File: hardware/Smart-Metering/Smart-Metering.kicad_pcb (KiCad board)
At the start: 4 copper layers, 130 x 130 mm, 230 parts, among them J101 AUX L N, J201 VA VB VC VN, J301 SENSOR_IA, J302 SENSOR_IB, J303 SENSOR_IC, J304 SENSOR_IN, J501 SWD, J701 HMI_LINK, J801 RS485, J802 USB-C, J901 BATTERY_1S, Q901 AO3401A, Q902 2N7002, SW901 POWER, U401 ADE9430ACPZ, U501 STM32F413RHT6, U502 24LC64, U601 ISO7762DW, U602 ISO7761DW, U604 MCP3204, U605 TPS7A2033PDBVR, U606 ADuM6000, U801 ADM2587E, U802 USBLC6-2SC6, U901 BQ25895RTW, U902 TPS63001, U903 TPS61022, Y401 24.576MHz, Y501 8MHz, Y502 32.768kHz

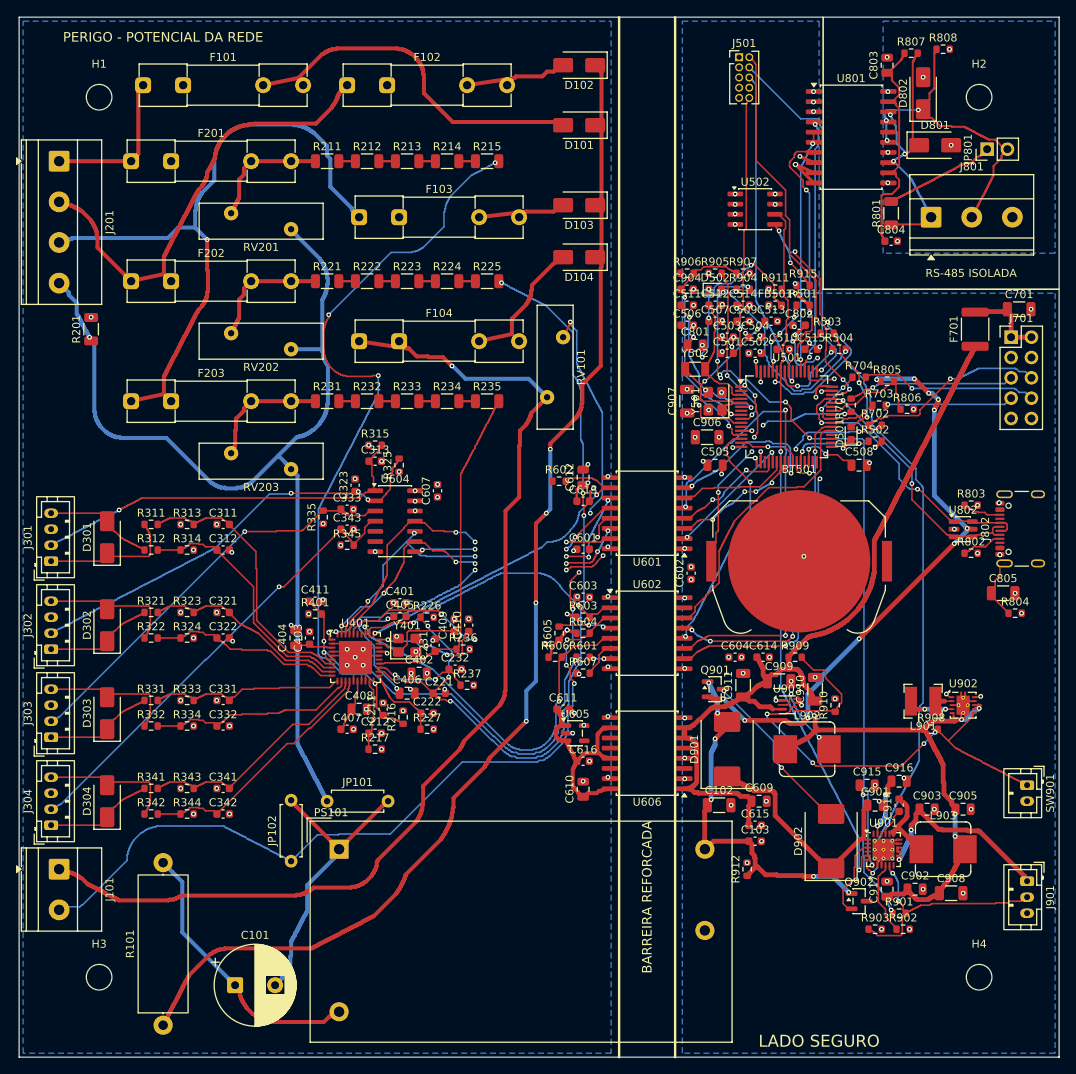
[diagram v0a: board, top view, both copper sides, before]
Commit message: Liga mais 8 pads pendentes da placa e atualiza a documentação
- reparo com vias menores (0,45/0,2 mm, 12 na placa), trechos de potência
  estreitados e reparo por grupo de pinos vizinhos; rodadas com ordens
  embaralhadas para o domínio quente;
- pendentes: 18 -> 10 (2 no domínio quente, 8 no lado seguro/RS-485),
  listados em docs/LAYOUT.md para ligar à mão;
- verificação geométrica da placa inteira: 0 violações; menor distância
  quente-seguro através da barreira: 8,02 mm;
- docs/LAYOUT.md: imagens da rev. 0.4 e seção de modelos 3D.

Co-Authored-By: Claude Opus 5.5 <noreply@anthropic.com>
Claude-Session: https://claude.ai/code/session_012B8cVkhtjf3eg98UdpNCpf
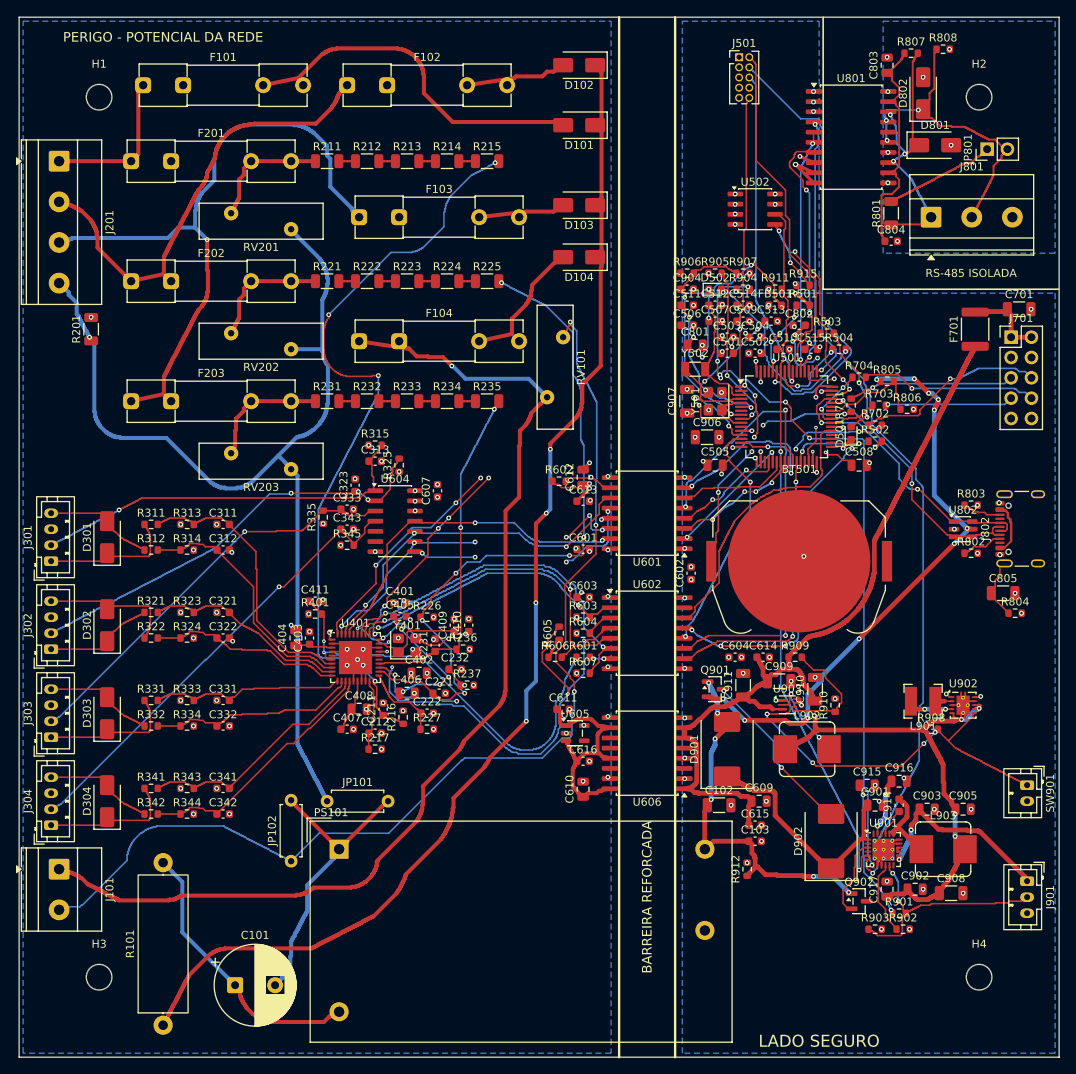
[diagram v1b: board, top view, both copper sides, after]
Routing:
- net ZX_ADE: track 6.49 -> 66.0 mm, vias 2 -> 5
- net CF2_ADE: track 4.38 -> 46.2 mm, vias 0 -> 2
- net DREADY_ADE: track 36.3 -> 3.30 mm, vias 3 -> 0
- net VBP: track 104.2 -> 88.1 mm
- net VBUS: track 74.1 -> 81.0 mm
- net VCN: track 12.5 -> 18.2 mm, vias 2 -> 3
- net CF1_ADE: track 49.2 -> 44.8 mm
- net /Metrology MCU/VCAP: track 8.10 -> 12.3 mm
- net MCU_RESET_ADE: track 40.7 -> 36.6 mm, vias 3 -> 2
- net MISO_ADE: track 48.5 -> 44.7 mm, vias 6 -> 3
- net Net-(D303-Pad2): track 17.1 -> 13.8 mm
- net Net-(D303-Pad1): track 13.8 -> 17.1 mm
- net Net-(D304-Pad1): track 13.8 -> 17.1 mm
- net Net-(D304-Pad2): track 17.1 -> 13.8 mm
- net /Isolation/SS_SID: track 26.8 -> 30.0 mm
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
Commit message: Integra a mecânica (modelo 3D) e os documentos do branch minhas-alteracoes (#3)
* Integra a mecânica e os documentos do branch minhas-alteracoes na main

- pasta 'modelo 3D/' (Onshape e Fusion: montagens, STEP, scripts); os
  FeatureScripts de cad/ passam para 'modelo 3D/Onshape/' sem alteração;
- AGENTS.md e docs DECISIONS, INTERNAL_BATTERY, POWER_CLOCK,
  VOLTAGE_SENSING, WORKFLOW, REVIEW_2026-10-02 e UPS_AUTONOMY, atualizados
  para o esquemático e o layout da main (divisor 5x200k+1k, ADuM6000 +
  TPS7A2033, BQ25895 + J901, RAC20); a versão anterior fica como histórico;
- decisão D-005 aplicada: Y401 ABM8-24.576MHZ-8-D1X-T (CL 8 pF) e
  C409/C410 de 10 pF C0G (antes 18 pF), no esquemático e na placa;
- novas decisões D-007 a D-011 e REQ-011 (alimentação e bateria interna);
  pendência P1: ~CE do BQ25895 em GND (carga habilitada antes do firmware).

A folha 10_Battery_Interface do branch não entra: a interface da bateria
já é o J901 da folha 09.

Co-Authored-By: Claude Opus 5.5 <noreply@anthropic.com>
Claude-Session: https://claude.ai/code/session_012B8cVkhtjf3eg98UdpNCpf

* Corrige os scripts do Fusion apontados na revisão do PR #3

- Exporta todos os STEP antes de ocultar carcaça e painel (os dois saíam vazios).
- Pasta do Fusion derivada da posição do script, sem caminho F:\ fixo.
- Posições e rotações lidas de mounting.json.
- Relatório e mensagem informam pares de interferência não verificados.
- Registra os STEP vazios da exportação atual e corrige espaços em UPS_AUTONOMY.

Co-Authored-By: Claude Opus 5.5 <noreply@anthropic.com>
Claude-Session: https://claude.ai/code/session_012B8cVkhtjf3eg98UdpNCpf

---------

Co-authored-by: Claude <noreply@anthropic.com>
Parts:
- C409, C410: value 18pF -> 10pF
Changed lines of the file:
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@@
 			)
 		)
-		(property "Value" "18pF"
+		(property "Value" "10pF"
 			(at 0 1.43 90)
 			(layer "F.Fab")
@@
 			)
 		)
-		(property "Value" "18pF"
+		(property "Value" "10pF"
 			(at 0 1.43 90)
 			(layer "F.Fab")

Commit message: Liga todas as ligações pendentes da placa (rev. 0.5)
- Liga os 10 pads pendentes e mais 5 ligações abertas achadas por uma
  verificação de conectividade (VSYS, VBUS, HSE_IN, VDDA, +3V3_ADE).
- Roteador local em grade de 0,05 mm com remoção e refazimento das trilhas
  vizinhas nos pinos de passo fino; 0 violações na verificação geométrica
  e 8,02 mm mínimos através da barreira.
- Regras: vias de 0,45/0,2 mm aceitas no .kicad_pro; trilhas POWER com
  mínimo de 0,2 mm (ótimo 0,6 mm) para os estreitamentos nos CIs.
- LAYOUT rev. 0.5 com as imagens novas e os pontos a revisar (VSYS, SW_5V).

Co-Authored-By: Claude Opus 5.5 <noreply@anthropic.com>
Claude-Session: https://claude.ai/code/session_012B8cVkhtjf3eg98UdpNCpf
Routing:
- net /Power Supplies/VBAT: track 25.2 -> 108.6 mm, vias 2 -> 12
- net CHG_N: track 21.3 -> 86.4 mm, vias 2 -> 8
- net DREADY_ADE: track 3.30 -> 43.2 mm, vias 0 -> 6
- net MCU_IRQ1: track 0.00 -> 24.3 mm, vias 0 -> 3
- net RESET_ADE: track 54.3 -> 75.6 mm, vias 3 -> 7
- net /Metrology MCU/NRST: track 28.5 -> 42.0 mm, vias 0 -> 4
- net /Power Supplies/CHG_DP: track 0.00 -> 8.74 mm, vias 0 -> 2
- net /Metrology MCU/HSE_IN: track 3.01 -> 9.90 mm, vias 0 -> 3
- net MCU_CF2: track 42.5 -> 48.0 mm, vias 2 -> 4
- net /ADE9430/AVDDOUT: track 17.4 -> 22.8 mm, vias 4 -> 5
- net VBUS: track 81.0 -> 86.3 mm, vias 11 -> 12
- net MCU_CF1: track 30.8 -> 35.9 mm, vias 2 -> 3
- net /Metrology MCU/VBAT_RTC: track 35.8 -> 40.9 mm, vias 7 -> 10
- net +3V3_ADE: track 13.8 -> 18.3 mm, vias 22 -> 24
- net HMI_TX: track 18.1 -> 22.5 mm
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
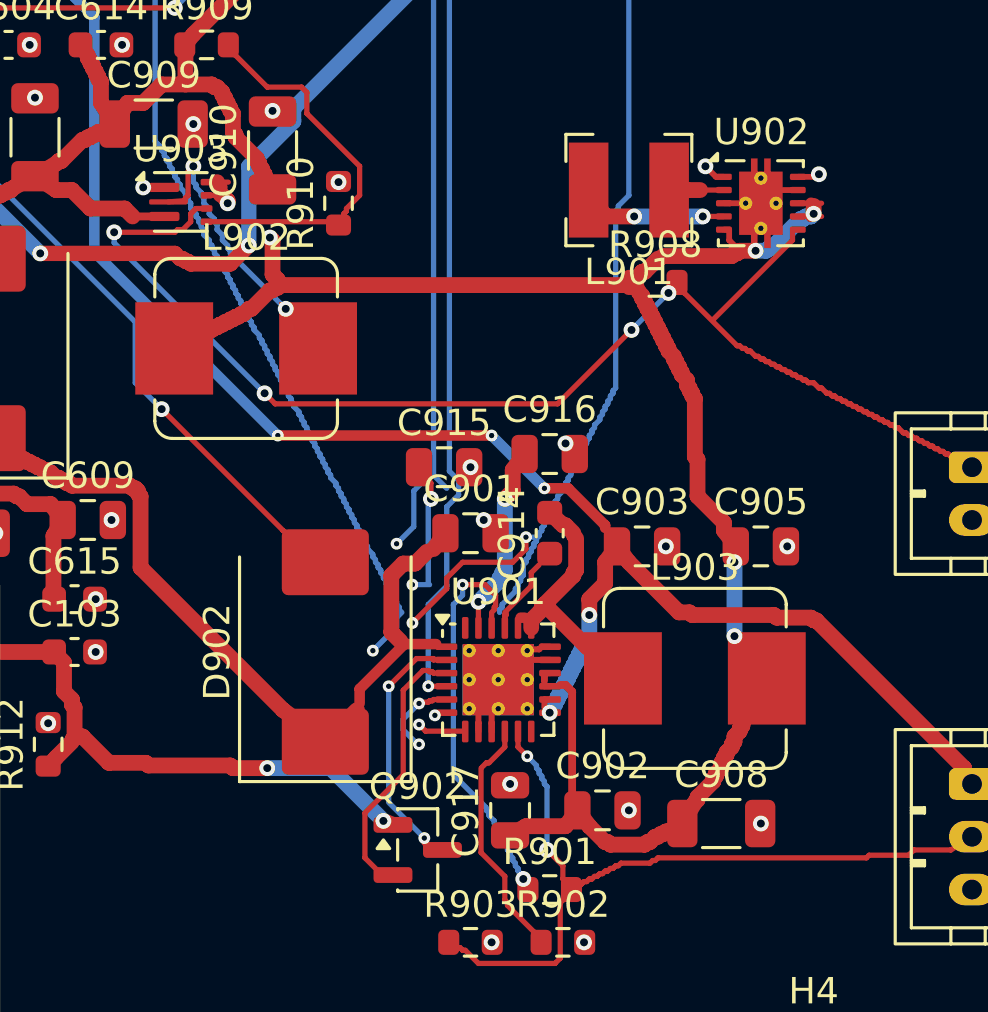
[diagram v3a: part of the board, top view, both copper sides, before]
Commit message: Alarga as trilhas de VSYS e SW_5V e acrescenta caminho paralelo de VSYS na B.Cu
Resposta à revisão do PR #4. As duas trilhas foram alargadas até o limite
das distâncias; a saída SYS do U901 ganhou um caminho de 1,2 mm na B.Cu com
4 vias. O SW_5V continua estreito e depende de aproximar L902 do U903
(registrado no LAYOUT como correção antes de fabricar).

Co-Authored-By: Claude Opus 5.5 <noreply@anthropic.com>
Claude-Session: https://claude.ai/code/session_012B8cVkhtjf3eg98UdpNCpf
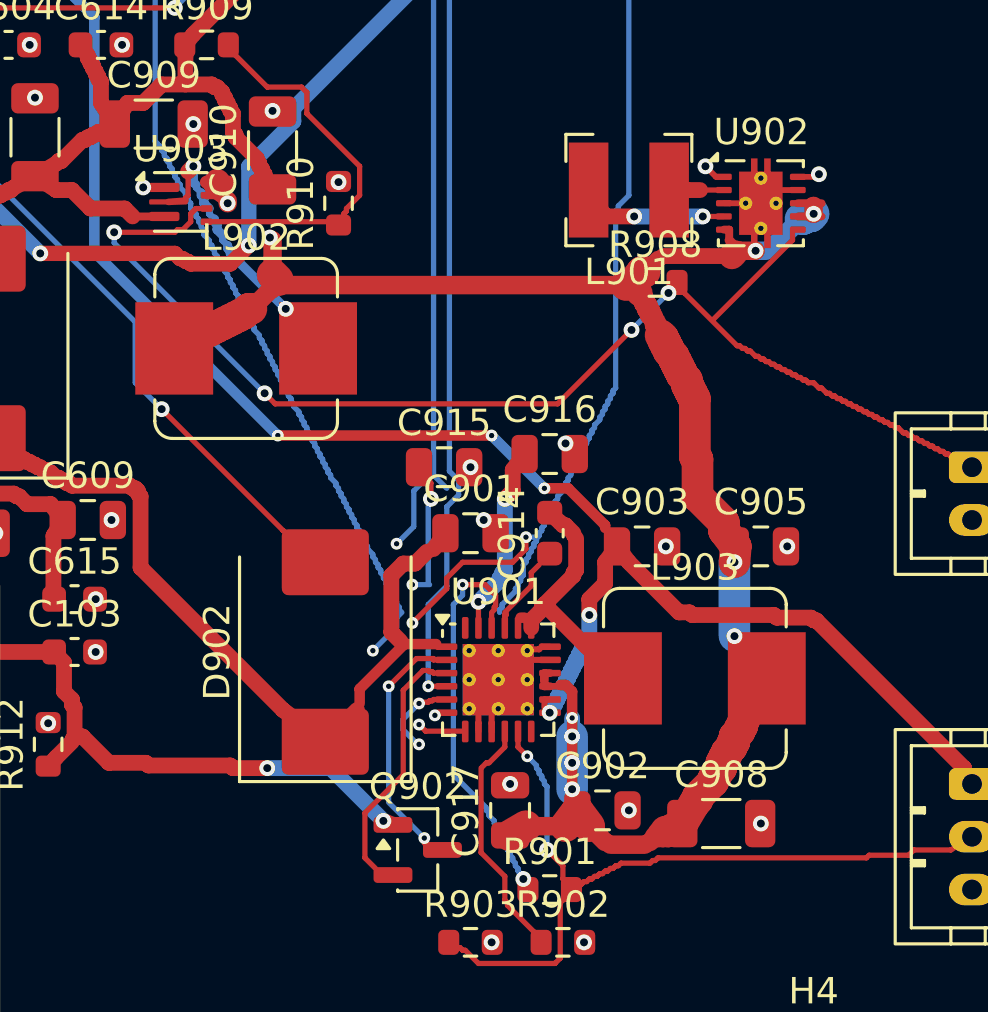
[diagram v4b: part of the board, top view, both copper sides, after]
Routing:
- net /Power Supplies/VSYS: track 73.1 -> 75.8 mm, vias 6 -> 10
